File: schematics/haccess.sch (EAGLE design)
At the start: 43 parts, among them IC1 ATMEGA32U2-TQFP, IC2 REG1117, Q2 BSS123, SW1 SPST_TACT-EVQQ2

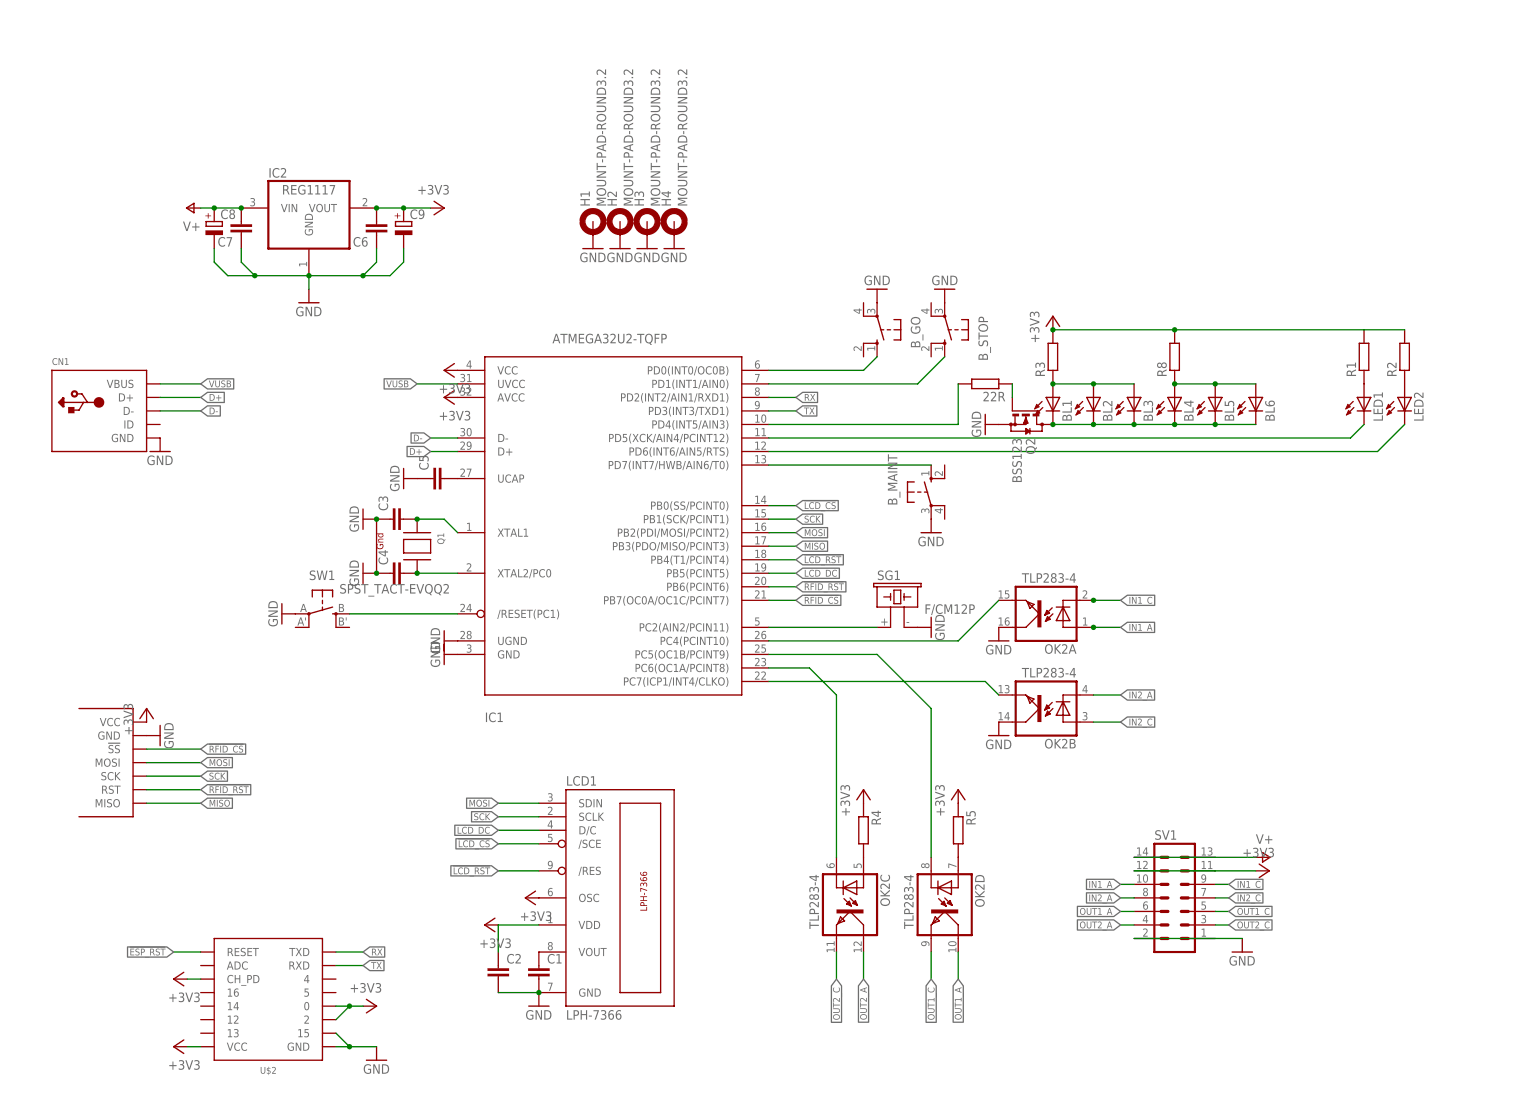
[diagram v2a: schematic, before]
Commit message: Routed board
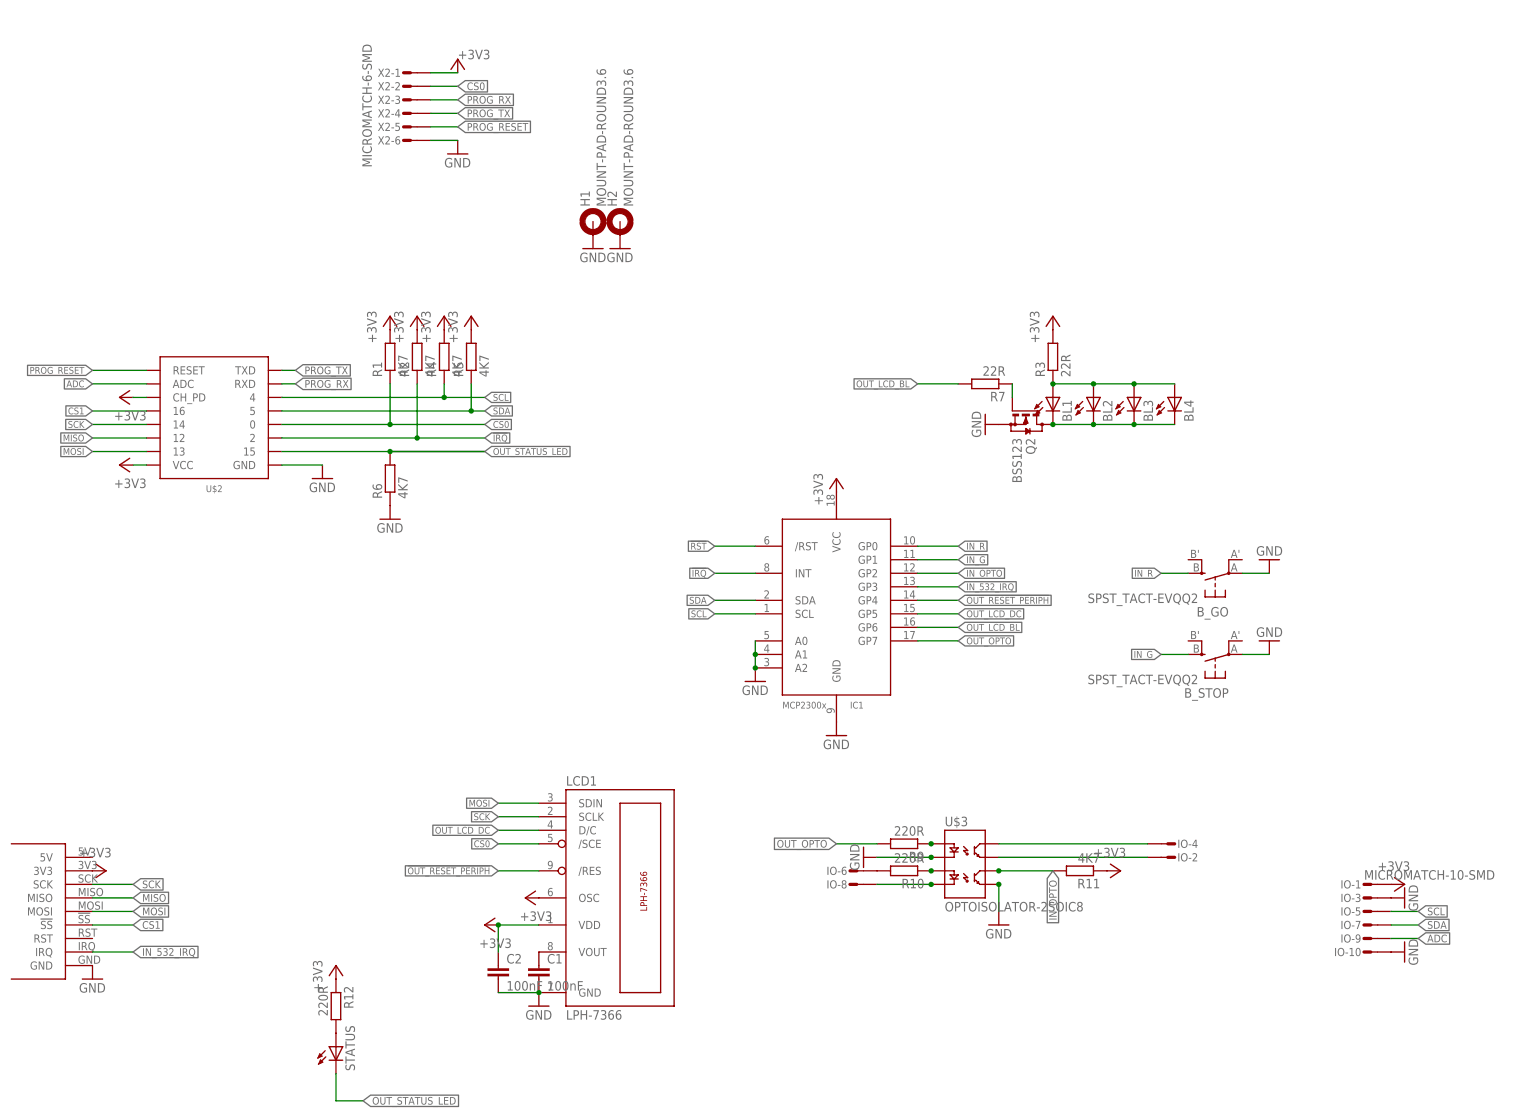
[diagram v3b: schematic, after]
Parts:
- removed 22R, R8: (no value), rcl:R-EU_R0805
- removed BL5, BL6, LED1, LED2: (no value), led:LEDCHIP-LED0805
- removed B_MAINT: (no value), switch-omron:40-XX
- removed C3, C4, C5, C6, C7: (no value), rcl:C-EUC0805K
- removed C8, C9: (no value), rcl:CPOL-EU153CLV-0405
- removed CN1: (no value), adafruit:USBMOLEX
- removed H3, H4: MOUNT-PAD-ROUND3.2, holes:MOUNT-PAD-ROUND3.2
- removed IC2: REG1117, burr-brown:REG1117
- removed OK2: TLP283-4, optocoupler:TLP283-4
- removed Q1: (no value), adafruit:XTAL-4-3225
- removed SG1: F/CM12P, buzzer:F/CM12P
- removed SV1: (no value), con-lstb:MA07-2
- removed SW1: SPST_TACT-EVQQ2, adafruit:SPST_TACT-EVQQ2
- added IO: MICROMATCH-10-SMD, tyco:MICROMATCH-10-SMD
- added R10, R12, R9: 220R, rcl:R-EU_R0603
- added R11, R6: 4K7, rcl:R-EU_R0603
- added R7: 22R, rcl:R-EU_R0603
- added STATUS: (no value), led:LEDCHIP-LED0805
- added U$3: OPTOISOLATOR-2SOIC8, SparkFun-DiscreteSemi:OPTOISOLATOR-2SOIC8
- added X2: MICROMATCH-6-SMD, tyco:MICROMATCH-6-SMD
- BL1, BL2, BL3, BL4: device led:LEDCHIP-LED0805 -> led:LEDCHIPLED_0603
- B_GO, B_STOP: value (none) -> SPST_TACT-EVQQ2; device switch-omron:40-XX -> adafruit:SPST_TACT-EVQQ2
- C1, C2: value (none) -> 100nF
- H1, H2: value MOUNT-PAD-ROUND3.2 -> MOUNT-PAD-ROUND3.6; device holes:MOUNT-PAD-ROUND3.2 -> holes:MOUNT-PAD-ROUND3.6
- IC1: value ATMEGA32U2-TQFP -> MCP2300X/SO; device adafruit:ATMEGA32U2-TQFP -> adafruit:MCP2300X/SO
- R1, R2, R4, R5: value (none) -> 4K7; device rcl:R-EU_R0805 -> rcl:R-EU_R0603
- R3: value (none) -> 22R; device rcl:R-EU_R0805 -> rcl:R-EU_R0603
- U$1: value FM1701 -> PN532SMALLMODULE; device FM1701:FM1701 -> PN532:PN532SMALLMODULE
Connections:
- removed net !ESP_RST: U$2.RESET
- removed net !LCD_CS: IC1.PB0(SS/PCINT0), LCD1./SCE
- removed net !LCD_RST: IC1.PB4(T1/PCINT4), LCD1./RES
- removed net !RFID_CS: IC1.PB7(OC0A/OC1C/PCINT7), U$1.!SS
- removed net !RFID_RST: IC1.PB6(PCINT6), U$1.RST
- removed net D+: CN1.D+, IC1.D+
- removed net D-: CN1.D-, IC1.D-
- removed net IN1_A: OK2A.A, SV1.10
- removed net IN1_C: OK2A.C, SV1.9
- removed net IN2_A: OK2B.C, SV1.8
- removed net IN2_C: OK2B.A, SV1.7
- removed net LCD_DC: IC1.PB5(PCINT5), LCD1.D/C
- removed net N$10: IC1.PC6(OC1A/PCINT8), OK2C.C
- removed net N$11: OK2D.C
- removed net N$12: C5.2, IC1.UCAP
- removed net N$13: IC1.PC7(ICP1/INT4/CLKO), OK2B.EMIT
- removed net N$14: B_MAINT.S, IC1.PD7(INT7/HWB/AIN6/T0)
- removed net N$15: IC1.PC4(PCINT10), OK2A.EMIT
- removed net N$16: OK2D.A, R5.2
- removed net N$17: LED2.A, R2.1
- removed net N$20: OK2C.A, R4.2
- removed net N$21: 22R.2, IC1.PD4(INT5/AIN3)
- removed net N$23: BL4.A, BL5.A, BL6.A, R8.1
- removed net N$24: IC1.PC2(AIN2/PCIN11), SG1.1
- removed net N$5: B_GO.S, IC1.PD0(INT0/OC0B)
- removed net N$6: B_STOP.S, IC1.PD1(INT1/AIN0)
- removed net N$7: IC1./RESET(PC1), SW1.S
- removed net OUT1_A: OK2D.COL, SV1.6
- removed net OUT1_C: OK2D.EMIT, SV1.5
- removed net OUT2_A: OK2C.COL, SV1.4
- removed net OUT2_C: OK2C.EMIT, SV1.3
- removed net RX: IC1.PD2(INT2/AIN1/RXD1), U$2.TXD
- removed net TX: IC1.PD3(INT3/TXD1), U$2.RXD
- removed net V+: C7.2, C8.+, IC2.VIN, SV1.13, SV1.14
- removed net VUSB: CN1.VBUS, IC1.UVCC
- new net !IRQ: IC1.INT, R2.1, U$2.2
- new net !OUT_RESET_PERIPH: IC1.GP4, LCD1./RES
- new net !RST: IC1./RST
- new net ADC: IO-9.S, U$2.ADC
- new net CS0: LCD1./SCE, R1.1, U$2.0, X2-2.S
- new net CS1: U$1.!SS, U$2.16
- new net IN_532_IRQ: IC1.GP3, U$1.IRQ
- new net IN_G: B_STOP.S, IC1.GP1
- new net IN_OPTO: IC1.GP2, R11.2, U$3.CL2
- new net IN_OPTO_A: IO-6.S, R10.2
- new net IN_OPTO_C: IO-8.S, U$3.C2
- new net IN_R: B_GO.S, IC1.GP0
- new net OUT_LCD_BL: IC1.GP6, R7.2
- new net OUT_LCD_DC: IC1.GP5, LCD1.D/C
- new net OUT_OPTO: IC1.GP7, R9.2
- new net OUT_STATUS_LED: R6.2, STATUS.C, U$2.15
- new net PROG_RESET: U$2.RESET, X2-5.S
- new net PROG_RX: U$2.RXD, X2-3.S
- new net PROG_TX: U$2.TXD, X2-4.S
- new net SCL: IC1.SCL, IO-5.S, R4.1, U$2.4
- new net SDA: IC1.SDA, IO-7.S, R5.1, U$2.5
- net +3V3: now also IO-1.S, R11.1, R12.1, R4.2, R5.2, U$1.3V3, X2-1.S; no longer C6.2, C9.+, IC1.AVCC, IC2.VOUT, R4.1, R5.1, R8.2, SV1.11, SV1.12, U$1.VCC, U$2.0, U$2.2
- net GND: now also IC1.A0, IC1.A1, IC1.A2, IO-10.S, IO-3.S, R6.1, U$3.C1, U$3.EM2, X2-6.S; no longer B_MAINT.P, C3.1, C4.1, C5.1, C6.1, C7.1, C8.-, C9.-, CN1.GND, H3.MOUNT, H4.MOUNT, IC1.UGND, IC2.GND, OK2A.COL, OK2B.COL, Q1.G1, Q1.G2, SG1.2, SV1.1, SV1.2, SW1.P, U$2.15
- net MISO: now also U$2.12; no longer IC1.PB3(PDO/MISO/PCINT3)
- net MOSI: now also U$2.13; no longer IC1.PB2(PDI/MOSI/PCINT2)
- net N$18: no longer BL5.C, BL6.C
- net N$19: now also BL4.A
- net N$2: now also R12.2, STATUS.A; no longer IC1.PD5(XCK/AIN4/PCINT12), LED1.C
- net N$22: now also R7.1; no longer 22R.1
- net N$3: now also R9.1, U$3.A1; no longer IC1.PD6(INT6/AIN5/RTS), LED2.C
- net N$4: now also R10.1, U$3.A2; no longer LED1.A, R1.1
- net N$8: now also IO-4.S, U$3.CL1; no longer C4.2, IC1.XTAL2/PC0, Q1.X2
- net N$9: now also IO-2.S, U$3.EM1; no longer C3.2, IC1.XTAL1, Q1.X1
- net SCK: now also U$2.14; no longer IC1.PB1(SCK/PCINT1)
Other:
- note removed: "2x Optoisolated Inputs"
- note removed: "2x Optoisolated Outputs"
- note removed: "ESP8266 talking MQTT / HTTPS"
- note removed: "FM1701 RFID Module"
- note removed: "OK and FAIL LEDs"
- note removed: "OPTIONAL VREG for 5v devices"
- note removed: "PROG USB port"
- note removed: "TODO: USB Protection"
- note removed: "TODO: replace with FM1701 chip + support"
- moved on the sheet: R1, R2, R4, R5, U$2

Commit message: Added extra decoupling caps to ESP and MCP, added resistor to IRQ line, increased size of +3V3 lines, improved routing, fixed ground plane under ESP, changed switches to SKPMAPE010
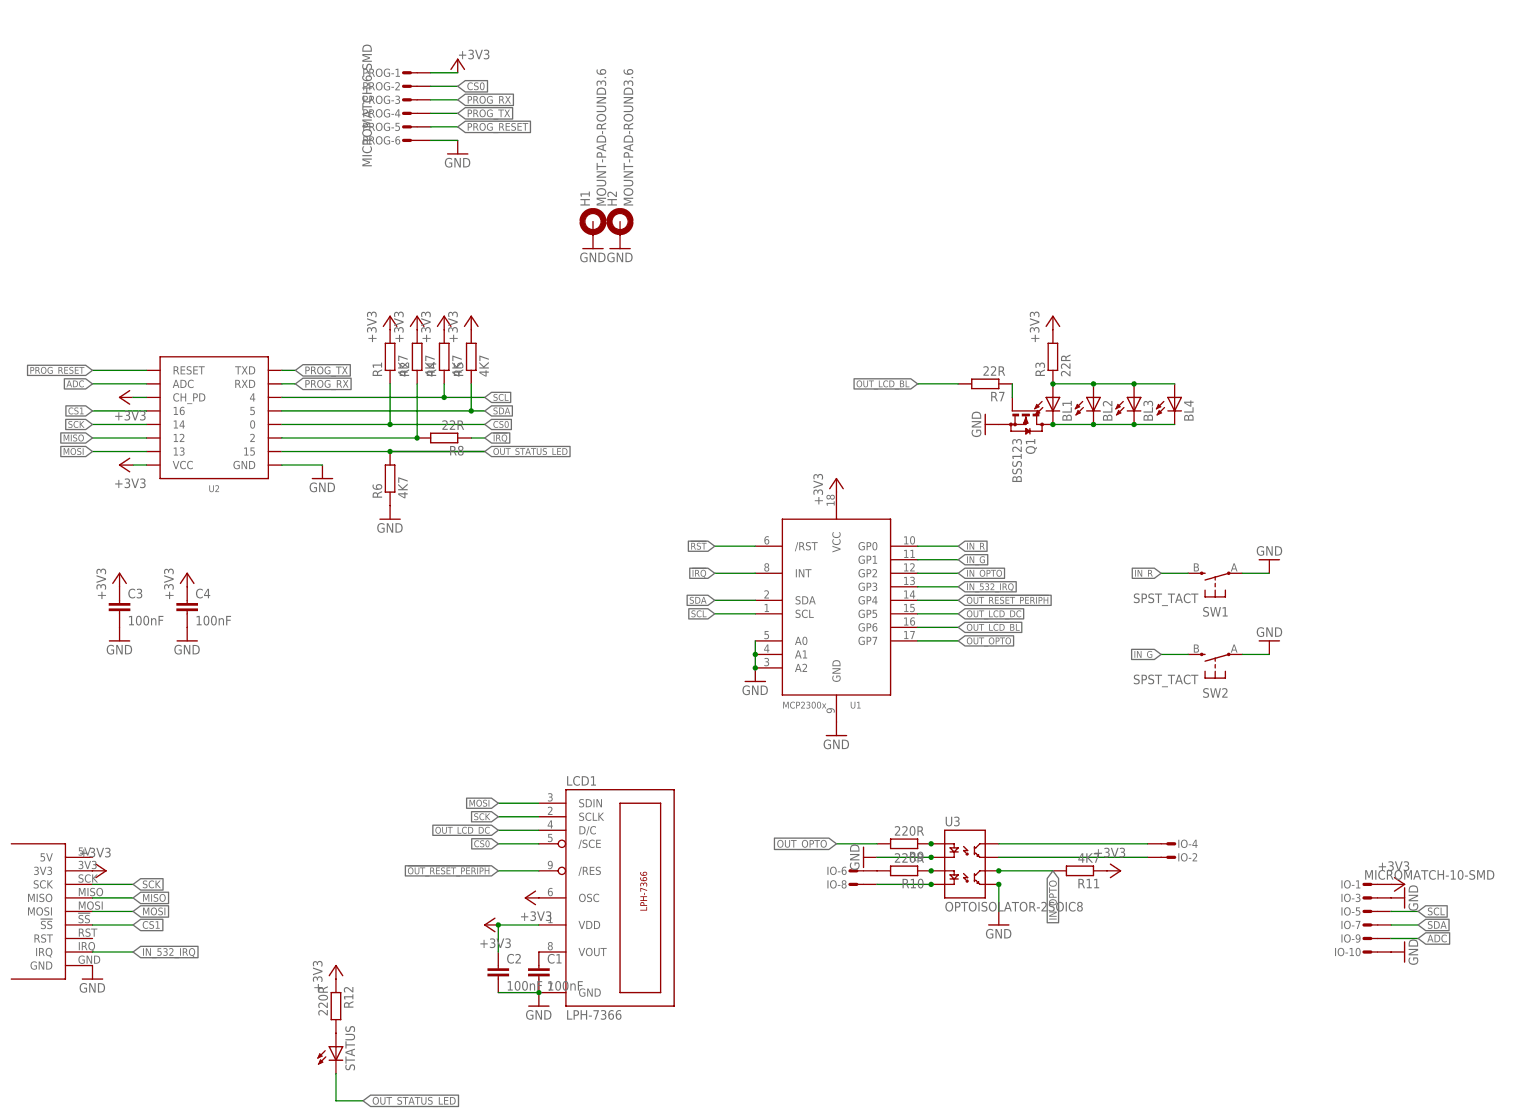
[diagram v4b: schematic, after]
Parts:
- removed B_GO, B_STOP: SPST_TACT-EVQQ2, adafruit:SPST_TACT-EVQQ2
- added C3, C4: 100nF, rcl:C-EUC0805K
- added R8: 22R, rcl:R-EU_R0603
- added SW1, SW2: SPST_TACT, smtswitch:SPST_TACT
- renumbered IC1 to U1, Q2 to Q1, U$2 to U2, U$3 to U3, X2 to PROG
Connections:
- new net !IRQ_1: R2.1, R8.2, U2.2
- net !IRQ: now also R8.1; no longer R2.1, U2.2
- net +3V3: now also C3.1, C4.1
- net GND: now also C3.2, C4.2, SW1.P, SW2.P; no longer B_GO.P, B_STOP.P
- net IN_G: now also SW2.S; no longer B_STOP.S
- net IN_R: now also SW1.S; no longer B_GO.S

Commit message: Added tant cap, increased size of 3V lines, improved documentation silks
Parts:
- added C5: (no value), rcl:CPOL-EUSMCB
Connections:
- net +3V3: now also C5.+
- net GND: now also C5.-
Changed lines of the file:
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@@
 </variantdefs>
 <classes>
-<class number="0" name="default" width="0" drill="0">
+<class number="0" name="Signal" width="0.3048" drill="0">
+</class>
+<class number="1" name="Power" width="0.6096" drill="0">
+<clearance class="1" value="0.254"/>
 </class>
 </classes>
@@
 <part name="SW1" library="smtswitch" deviceset="SPST_TACT" device=""/>
 <part name="SW2" library="smtswitch" deviceset="SPST_TACT" device=""/>
+<part name="C5" library="rcl" deviceset="CPOL-EU" device="SMCB"/>
+<part name="+3V18" library="supply1" deviceset="+3V3" device=""/>
+<part name="GND14" library="supply1" deviceset="GND" device=""/>
 </parts>
 <sheets>
@@
 <instance part="SW1" gate="G$1" x="198.12" y="129.54" rot="R90"/>
 <instance part="SW2" gate="G$1" x="198.12" y="114.3" rot="R90"/>
+<instance part="C5" gate="G$1" x="17.78" y="124.46"/>
+<instance part="+3V18" gate="G$1" x="17.78" y="129.54"/>
+<instance part="GND14" gate="1" x="17.78" y="116.84"/>
 </instances>
 <busses>
@@
 <pinref part="GND15" gate="1" pin="GND"/>
 </segment>
-</net>
-<net name="+3V3" class="0">
+<segment>
+<pinref part="C5" gate="G$1" pin="-"/>
+<pinref part="GND14" gate="1" pin="GND"/>
+</segment>
+</net>
+<net name="+3V3" class="1">
 <segment>
 <pinref part="U2" gate="G$1" pin="VCC"/>
@@
 <pinref part="+3V17" gate="G$1" pin="+3V3"/>
 </segment>
+<segment>
+<pinref part="C5" gate="G$1" pin="+"/>
+<pinref part="+3V18" gate="G$1" pin="+3V3"/>
+</segment>
 </net>
 <net name="N$1" class="0">
@@
 </segment>
 </net>
-<net name="N$18" class="0">
+<net name="N$18" class="1">
 <segment>
 <pinref part="BL1" gate="G$1" pin="C"/>
@@
 </segment>
 </net>
-<net name="N$19" class="0">
+<net name="N$19" class="1">
 <segment>
 <pinref part="BL1" gate="G$1" pin="A"/>
